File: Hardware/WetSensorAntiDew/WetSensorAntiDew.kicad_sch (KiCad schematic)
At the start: 9 parts

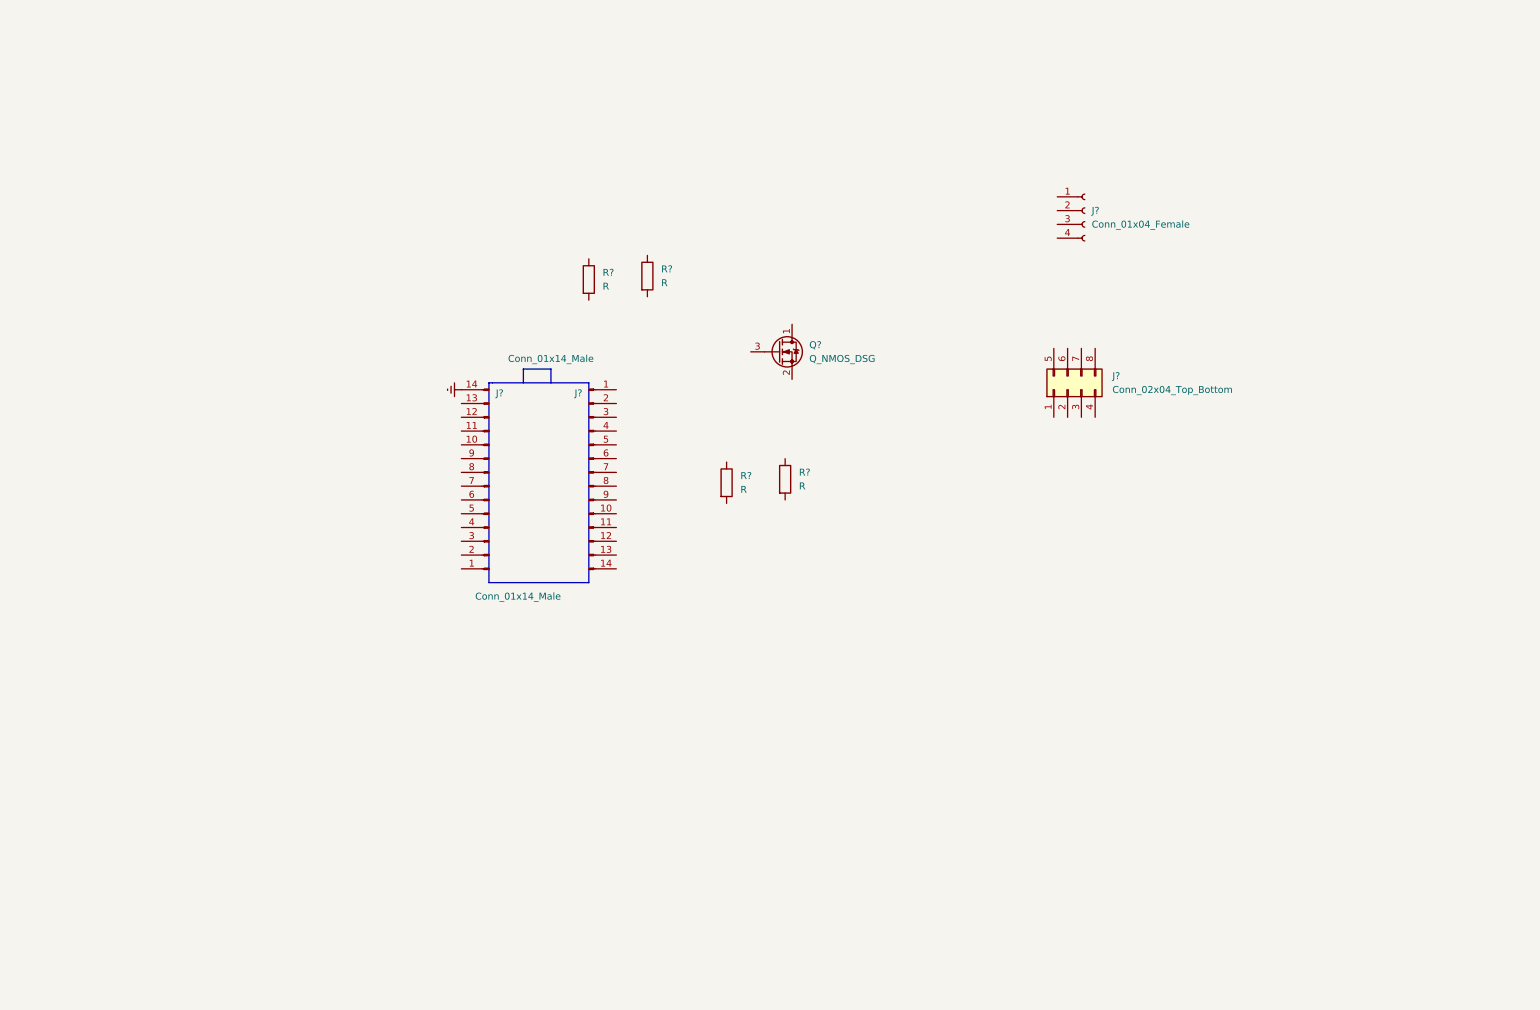
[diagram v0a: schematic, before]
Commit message: First schematic of HeatedWetSensorPCB
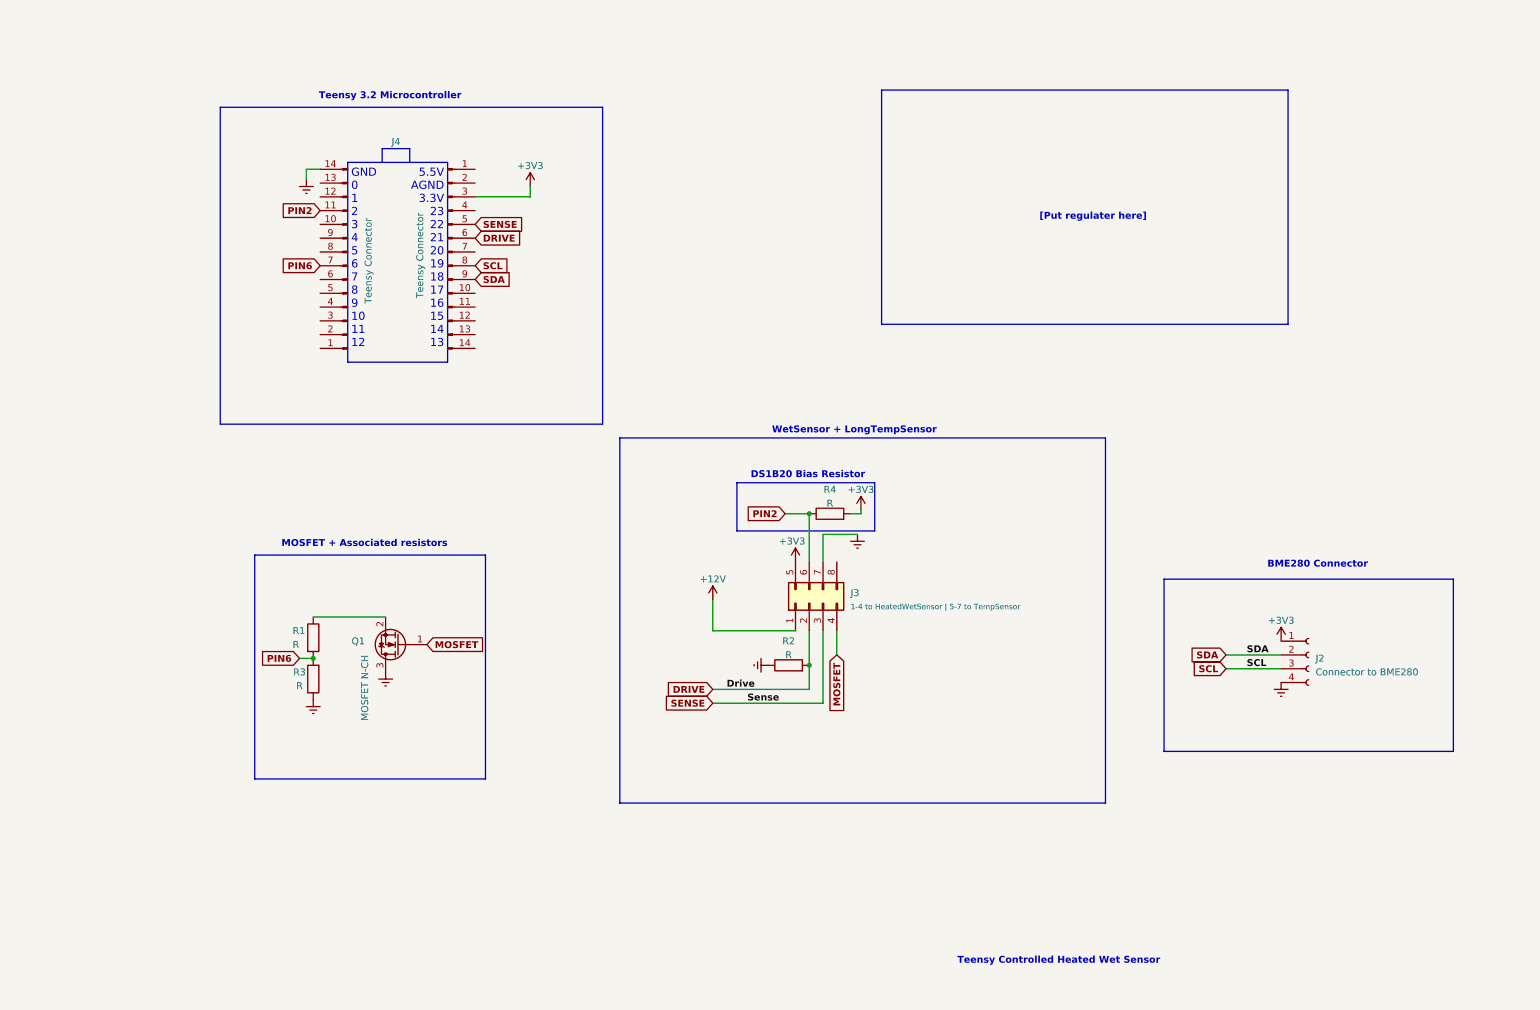
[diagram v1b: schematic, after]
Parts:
- removed J?: Conn_01x14_Male, Connector_PinHeader_2.54mm:PinHeader_1x14_P2.54mm_Vertical, symbol Connector:Conn_01x14_Male
- removed J?: Conn_01x14_Male, symbol Connector:Conn_01x14_Male
- removed Q?: Q_NMOS_DSG, symbol Device:Q_NMOS_DSG
- removed R?: R, Resistor_SMD:R_0402_1005Metric_Pad0.72x0.64mm_HandSolder, symbol Device:R
- added J1, J4: Teensy Connector, Connector_PinHeader_2.54mm:PinHeader_1x14_P2.54mm_Vertical, symbol Connector:Conn_01x14_Male
- added Q1: MOSFET N-CH, Package_TO_SOT_SMD:SOT-23, symbol Transistor_FET:DMG2302U
- added R3: R, Resistor_SMD:R_0402_1005Metric_Pad0.72x0.64mm_HandSolder, symbol Device:R
- J2: renamed from J?; value Conn_01x04_Female -> Connector to BME280
- J3: renamed from J?; value Conn_02x04_Top_Bottom -> 1-4 to HeatedWetSensor | 5-7 to TempSensor
- R2: renamed from R?; footprint (none) -> Resistor_SMD:R_0402_1005Metric_Pad0.72x0.64mm_HandSolder
- gave numbers to parts that had none: 2
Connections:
- net Earth: now also J2.4 (Pin_4), J3.7 (Pin_7), R2.1, J1.14 (Pin_14), Q1.3 (D), R3.1
- net PIN2: now reaches R4.1
- net PIN2: now also J3.6 (Pin_6), J1.11 (Pin_11)
- net +3V3: now reaches R4.2
- net +3V3: now also J2.1 (Pin_1), J3.5 (Pin_5), J4.3 (Pin_3)
- net SDA: now reaches J2.2 (Pin_2)
- net SDA: now also J4.9 (Pin_9)
- net SCL: now reaches J2.3 (Pin_3)
- net SCL: now also J4.8 (Pin_8)
- net DRIVE: now reaches R2.2
- net DRIVE: now also J3.2 (Pin_2), J4.6 (Pin_6)
- net at R1.1: now also Q1.2 (S)
- net PIN6: now reaches R1.2
- net PIN6: now also J1.7 (Pin_7), R3.2
- net +12V: now reaches J3.1 (Pin_1)
- net SENSE: now reaches J3.3 (Pin_3)
- net SENSE: now also J4.5 (Pin_5)
- net MOSFET: now reaches J3.4 (Pin_4)
- net MOSFET: now also Q1.1 (G)
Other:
- note added: "5.5V AGND 3.3V 23 22 21 20 19 18 17 16 15 14 13"
- note added: "BME280 Connector"
- note added: "DS1B20 Bias Resistor"
- note added: "GND 0 1 2 3 4 5 6 7 8 9 10 11 12"
- note added: "MOSFET + Associated resistors"
- note added: "Teensy 3.2 Microcontroller"
- note added: "Teensy Controlled Heated Wet Sensor"
- note added: "WetSensor + LongTempSensor"
- note added: "[Put regulater here]"
- moved on the sheet: J2, J3, R1, R2, R4

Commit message: abc
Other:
- note added: "AMOGUS"
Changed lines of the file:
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@@
     (effects (font (size 1.27 1.27) (thickness 0.254) bold) (justify left bottom))
+  )
+  (text "AMOGUS\n" (at 179.705 53.975 0)
+    (effects (font (size 1.27 1.27)) (justify left bottom))
   )
   (label "SCL" (at 240.665 135.89 0) (fields_autoplaced)

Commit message: Added Gatekeep
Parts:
- added C1: C, symbol Device:C
- added R5, R6: R, Resistor_SMD:R_0402_1005Metric_Pad0.72x0.64mm_HandSolder, symbol Device:R
- added U1: AMS1117, Package_TO_SOT_SMD:SOT-223-3_TabPin2, symbol Regulator_Linear:AMS1117
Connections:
- net +12V: now also R5.2, U1.2 (VO)
- net Earth: now also C1.2, R6.1
- new net: R5.1, R6.2, U1.1 (ADJ)
- new net: C1.1, U1.3 (VI)
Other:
- note added: "Gatekeep (Voltage Regulator)"
- note removed: "AMOGUS"
- note removed: "[Put regulater here]"
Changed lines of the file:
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@@
 (kicad_sch (version 20230121) (generator eeschema)
   (paper "A4")
+  (junction (at 238.125 46.99) (diameter 0) (color 0 0 0 0)
+  )
   (junction (at 160.02 107.315) (diameter 0) (color 0 0 0 0)
   )
   (junction (at 68.58 133.985) (diameter 0) (color 0 0 0 0)
+  )
+  (junction (at 238.125 54.61) (diameter 0) (color 0 0 0 0)
   )
   (junction (at 160.02 135.255) (diameter 0) (color 0 0 0 0)
@@
     (stroke (width 0) (type default))
   )
+  (wire (pts (xy 228.6 46.99) (xy 238.125 46.99))
+    (stroke (width 0) (type default))
+  )
   (wire (pts (xy 108.585 48.895) (xy 108.585 46.99))
     (stroke (width 0) (type default))
@@
     (stroke (width 0) (type solid))
   )
+  (wire (pts (xy 220.98 54.61) (xy 238.125 54.61))
+    (stroke (width 0) (type default))
+  )
   (wire (pts (xy 165.1 128.905) (xy 165.1 133.35))
     (stroke (width 0) (type default))
@@
     (stroke (width 0) (type default))
   )
+  (wire (pts (xy 206.375 46.99) (xy 206.375 50.165))
+    (stroke (width 0) (type default))
+  )
   (polyline (pts (xy 86.36 40.005) (xy 86.36 42.545))
     (stroke (width 0) (type solid))
@@
     (stroke (width 0) (type default))
   )
+  (wire (pts (xy 238.125 46.99) (xy 238.125 43.18))
+    (stroke (width 0) (type default))
+  )
   (wire (pts (xy 236.855 135.89) (xy 247.015 135.89))
     (stroke (width 0) (type default))
@@
     (stroke (width 0) (type default))
   )
+  (wire (pts (xy 213.36 46.99) (xy 206.375 46.99))
+    (stroke (width 0) (type default))
+  )
   (wire (pts (xy 236.855 133.35) (xy 247.015 133.35))
     (stroke (width 0) (type default))
@@
     (effects (font (size 1.27 1.27) bold) (justify left bottom))
   )
-  (text "[Put regulater here]" (at 222.25 53.34 0)
-    (effects (font (size 1.27 1.27) bold) (justify right bottom))
-  )
   (text "5.5V\nAGND\n3.3V\n23\n22\n21\n20\n19\n18\n17\n16\n15\n14\n13" (at 92.71 76.835 0)
     (effects (font (size 1.5 1.5)) (justify right bottom))
@@
     (effects (font (size 1.27 1.27) (thickness 0.254) bold) (justify left bottom))
   )
-  (text "AMOGUS\n" (at 179.705 53.975 0)
-    (effects (font (size 1.27 1.27)) (justify left bottom))
+  (text "Gatekeep (Voltage Regulator)" (at 200.025 28.575 0)
+    (effects (font (size 1.27 1.27) (thickness 0.254) bold) (justify left bottom))
   )
   (label "SCL" (at 240.665 135.89 0) (fields_autoplaced)
@@
         (path "/4d9ca3a9-89cf-4a0b-a8ab-770e84bd9292"
           (reference "J2") (unit 1)
+        )
+      )
+    )
+  )
+  (symbol (lib_id "Regulator_Linear:AMS1117") (at 220.98 46.99 0) (unit 1)
+    (in_bom yes) (on_board yes) (dnp no) (fields_autoplaced)
+    (property "Reference" "U1" (at 220.98 40.64 0)
+      (effects (font (size 1.27 1.27)))
+    )
+    (property "Value" "AMS1117" (at 220.98 43.18 0)
+      (effects (font (size 1.27 1.27)))
+    )
+    (property "Footprint" "Package_TO_SOT_SMD:SOT-223-3_TabPin2" (at 220.98 41.91 0)
+      (effects (font (size 1.27 1.27)) hide)
+    )
+    (property "Datasheet" "http://www.advanced-monolithic.com/pdf/ds1117.pdf" (at 223.52 53.34 0)
+      (effects (font (size 1.27 1.27)) hide)
+    )
+    (pin "1")
+    (pin "2")
+    (pin "3")
+    (instances
+      (project "WetSensorAntiDew"
+        (path "/4d9ca3a9-89cf-4a0b-a8ab-770e84bd9292"
+          (reference "U1") (unit 1)
+        )
+      )
+    )
+  )
+  (symbol (lib_id "Device:C") (at 206.375 53.975 0) (unit 1)
+    (in_bom yes) (on_board yes) (dnp no) (fields_autoplaced)
+    (property "Reference" "C1" (at 209.55 53.34 0)
+      (effects (font (size 1.27 1.27)) (justify left))
+    )
+    (property "Value" "C" (at 209.55 55.88 0)
+      (effects (font (size 1.27 1.27)) (justify left))
+    )
+    (property "Footprint" "" (at 207.3402 57.785 0)
+      (effects (font (size 1.27 1.27)) hide)
+    )
+    (property "Datasheet" "~" (at 206.375 53.975 0)
+      (effects (font (size 1.27 1.27)) hide)
+    )
+    (pin "1")
+    (pin "2")
+    (instances
+      (project "WetSensorAntiDew"
+        (path "/4d9ca3a9-89cf-4a0b-a8ab-770e84bd9292"
+          (reference "C1") (unit 1)
+        )
+      )
+    )
+  )
+  (symbol (lib_id "power:+12V") (at 238.125 43.18 0) (unit 1)
+    (in_bom yes) (on_board yes) (dnp no) (fields_autoplaced)
+    (property "Reference" "#PWR011" (at 238.125 46.99 0)
+      (effects (font (size 1.27 1.27)) hide)
+    )
+    (property "Value" "+12V" (at 238.125 39.37 0)
+      (effects (font (size 1.27 1.27)))
+    )
+    (property "Footprint" "" (at 238.125 43.18 0)
+      (effects (font (size 1.27 1.27)) hide)
+    )
+    (property "Datasheet" "" (at 238.125 43.18 0)
+      (effects (font (size 1.27 1.27)) hide)
+    )
+    (pin "1")
+    (instances
+      (project "WetSensorAntiDew"
+        (path "/4d9ca3a9-89cf-4a0b-a8ab-770e84bd9292"
+          (reference "#PWR011") (unit 1)
         )
       )
@@
     )
   )
+  (symbol (lib_id "Device:R") (at 238.125 50.8 180) (unit 1)
+    (in_bom yes) (on_board yes) (dnp no) (fields_autoplaced)
+    (property "Reference" "R5" (at 240.03 50.165 0)
+      (effects (font (size 1.27 1.27)) (justify right))
+    )
+    (property "Value" "R" (at 240.03 52.705 0)
+      (effects (font (size 1.27 1.27)) (justify right))
+    )
+    (property "Footprint" "Resistor_SMD:R_0402_1005Metric_Pad0.72x0.64mm_HandSolder" (at 239.903 50.8 90)
+      (effects (font (size 1.27 1.27)) hide)
+    )
+    (property "Datasheet" "~" (at 238.125 50.8 0)
+      (effects (font (size 1.27 1.27)) hide)
+    )
+    (pin "1")
+    (pin "2")
+    (instances
+      (project "WetSensorAntiDew"
+        (path "/4d9ca3a9-89cf-4a0b-a8ab-770e84bd9292"
+          (reference "R5") (unit 1)
+        )
+      )
+    )
+  )
   (symbol (lib_id "Device:R") (at 68.58 137.795 180) (unit 1)
     (in_bom yes) (on_board yes) (dnp no)
@@
         (path "/4d9ca3a9-89cf-4a0b-a8ab-770e84bd9292"
           (reference "#PWR?") (unit 1)
+        )
+      )
+    )
+  )
+  (symbol (lib_id "Device:R") (at 238.125 58.42 180) (unit 1)
+    (in_bom yes) (on_board yes) (dnp no) (fields_autoplaced)
+    (property "Reference" "R6" (at 240.03 57.785 0)
+      (effects (font (size 1.27 1.27)) (justify right))
+    )
+    (property "Value" "R" (at 240.03 60.325 0)
+      (effects (font (size 1.27 1.27)) (justify right))
+    )
+    (property "Footprint" "Resistor_SMD:R_0402_1005Metric_Pad0.72x0.64mm_HandSolder" (at 239.903 58.42 90)
+      (effects (font (size 1.27 1.27)) hide)
+    )
+    (property "Datasheet" "~" (at 238.125 58.42 0)
+      (effects (font (size 1.27 1.27)) hide)
+    )
+    (pin "1")
+    (pin "2")
+    (instances
+      (project "WetSensorAntiDew"
+        (path "/4d9ca3a9-89cf-4a0b-a8ab-770e84bd9292"
+          (reference "R6") (unit 1)
+        )
+      )
+    )
+  )
+  (symbol (lib_id "power:Earth") (at 206.375 57.785 0) (unit 1)
+    (in_bom yes) (on_board yes) (dnp no) (fields_autoplaced)
+    (property "Reference" "#PWR013" (at 206.375 64.135 0)
+      (effects (font (size 1.27 1.27)) hide)
+    )
+    (property "Value" "Earth" (at 206.375 61.595 0)
+      (effects (font (size 1.27 1.27)) hide)
+    )
+    (property "Footprint" "" (at 206.375 57.785 0)
+      (effects (font (size 1.27 1.27)) hide)
+    )
+    (property "Datasheet" "~" (at 206.375 57.785 0)
+      (effects (font (size 1.27 1.27)) hide)
+    )
+    (pin "1")
+    (instances
+      (project "WetSensorAntiDew"
+        (path "/4d9ca3a9-89cf-4a0b-a8ab-770e84bd9292"
+          (reference "#PWR013") (unit 1)
         )
       )
@@
         )
       )
+    )
+  )
+  (symbol (lib_id "power:Earth") (at 238.125 62.23 0) (unit 1)
+    (in_bom yes) (on_board yes) (dnp no) (fields_autoplaced)
+    (property "Reference" "#PWR012" (at 238.125 68.58 0)
+      (effects (font (size 1.27 1.27)) hide)
+    )
+    (property "Value" "Earth" (at 238.125 66.04 0)
+      (effects (font (size 1.27 1.27)) hide)
+    )
+    (property "Footprint" "" (at 238.125 62.23 0)
+      (effects (font (size 1.27 1.27)) hide)
+    )
+    (property "Datasheet" "~" (at 238.125 62.23 0)
+      (effects (font (size 1.27 1.27)) hide)
+    )
+    (pin "1")
+    (instances
+      (project "WetSensorAntiDew"
+        (path "/4d9ca3a9-89cf-4a0b-a8ab-770e84bd9292"
+          (reference "#PWR012") (unit 1)
+        )
+      )

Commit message: added connector to gatekeep for power supply
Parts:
- added J5: Connector to power supply, Connector_Phoenix_MSTB:PhoenixContact_MSTBA_2,5_2-G_1x02_P5.00mm_Horizontal, symbol Connector:Conn_01x02_Socket
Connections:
- net Earth: now also J5.1 (Pin_1)
- net at C1.1, U1.3 (VI): now also J5.2 (Pin_2)
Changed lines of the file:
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@@
   (junction (at 160.02 107.315) (diameter 0) (color 0 0 0 0)
   )
+  (junction (at 206.375 46.99) (diameter 0) (color 0 0 0 0)
+  )
   (junction (at 68.58 133.985) (diameter 0) (color 0 0 0 0)
   )
@@
     (stroke (width 0) (type default))
   )
+  (wire (pts (xy 192.405 46.99) (xy 206.375 46.99))
+    (stroke (width 0) (type default))
+  )
   (wire (pts (xy 66.04 133.985) (xy 68.58 133.985))
     (stroke (width 0) (type default))
@@
   (polyline (pts (xy 74.93 42.545) (xy 74.93 79.375))
     (stroke (width 0) (type solid))
+  )
+  (wire (pts (xy 192.405 42.545) (xy 192.405 46.99))
+    (stroke (width 0) (type default))
   )
   (wire (pts (xy 220.98 54.61) (xy 238.125 54.61))
@@
         (path "/4d9ca3a9-89cf-4a0b-a8ab-770e84bd9292"
           (reference "#PWR08") (unit 1)
+        )
+      )
+    )
+  )
+  (symbol (lib_id "power:Earth") (at 189.865 42.545 0) (unit 1)
+    (in_bom yes) (on_board yes) (dnp no) (fields_autoplaced)
+    (property "Reference" "#PWR014" (at 189.865 48.895 0)
+      (effects (font (size 1.27 1.27)) hide)
+    )
+    (property "Value" "Earth" (at 189.865 46.355 0)
+      (effects (font (size 1.27 1.27)) hide)
+    )
+    (property "Footprint" "" (at 189.865 42.545 0)
+      (effects (font (size 1.27 1.27)) hide)
+    )
+    (property "Datasheet" "~" (at 189.865 42.545 0)
+      (effects (font (size 1.27 1.27)) hide)
+    )
+    (pin "1")
+    (instances
+      (project "WetSensorAntiDew"
+        (path "/4d9ca3a9-89cf-4a0b-a8ab-770e84bd9292"
+          (reference "#PWR014") (unit 1)
         )
       )
@@
         )
       )
+    )
+  )
+  (symbol (lib_id "Connector:Conn_01x02_Socket") (at 189.865 37.465 90) (unit 1)
+    (in_bom yes) (on_board yes) (dnp no)
+    (property "Reference" "J5" (at 194.31 37.465 90)
+      (effects (font (size 1.27 1.27)) (justify right))
+    )
+    (property "Value" "Connector to power supply" (at 186.69 32.385 0)
+      (effects (font (size 1.27 1.27)) (justify right))
+    )
+    (property "Footprint" "Connector_Phoenix_MSTB:PhoenixContact_MSTBA_2,5_2-G_1x02_P5.00mm_Horizontal" (at 189.865 37.465 0)
+      (effects (font (size 1.27 1.27)) hide)
+    )
+    (property "Datasheet" "~" (at 189.865 37.465 0)
+      (effects (font (size 1.27 1.27)) hide)
+    )
+    (pin "1")
+    (pin "2")
+    (instances
+      (project "WetSensorAntiDew"
+        (path "/4d9ca3a9-89cf-4a0b-a8ab-770e84bd9292"
+          (reference "J5") (unit 1)
+        )
+      )

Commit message: added footprints and properly spaced teensy connectors
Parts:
- C1: footprint (none) -> Capacitor_SMD:C_0603_1608Metric_Pad1.08x0.95mm_HandSolder
- J2: footprint (none) -> Connector_PinSocket_2.54mm:PinSocket_1x04_P2.54mm_Horizontal
- J3: footprint (none) -> Connector_IDC:IDC-Header_2x04_P2.54mm_Horizontal
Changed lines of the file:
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@@
       (effects (font (size 1.27 1.27)) (justify left))
     )
-    (property "Footprint" "" (at 252.095 133.35 0)
+    (property "Footprint" "Connector_PinSocket_2.54mm:PinSocket_1x04_P2.54mm_Horizontal" (at 252.095 133.35 0)
       (effects (font (size 1.27 1.27)) hide)
     )
@@
       (effects (font (size 1.27 1.27)) (justify left))
     )
-    (property "Footprint" "" (at 207.3402 57.785 0)
+    (property "Footprint" "Capacitor_SMD:C_0603_1608Metric_Pad1.08x0.95mm_HandSolder" (at 207.3402 57.785 0)
       (effects (font (size 1.27 1.27)) hide)
     )
@@
   (symbol (lib_id "power:Earth") (at 67.31 45.72 0) (unit 1)
     (in_bom yes) (on_board yes) (dnp no) (fields_autoplaced)
-    (property "Reference" "#PWR?" (at 67.31 52.07 0)
+    (property "Reference" "#PWR0101" (at 67.31 52.07 0)
       (effects (font (size 1.27 1.27)) hide)
     )
@@
       (project "WetSensorAntiDew"
         (path "/4d9ca3a9-89cf-4a0b-a8ab-770e84bd9292"
-          (reference "#PWR?") (unit 1)
+          (reference "#PWR0101") (unit 1)
         )
       )
@@
       (effects (font (size 1 1)) (justify right))
     )
-    (property "Footprint" "" (at 160.02 123.825 0)
-      (effects (font (size 1.27 1.27)) hide)
-    )
+    (property "Footprint" "Connector_IDC:IDC-Header_2x04_P2.54mm_Horizontal" (at 160.02 123.825 0)
+      (effects (font (size 1.27 1.27)) hide)
+    )
